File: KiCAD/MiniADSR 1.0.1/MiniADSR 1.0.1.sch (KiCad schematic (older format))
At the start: 35 parts, among them J1 INPUT, J2 OUTPUT, J4 ControlBoard_Pins, J6 MainBoard_Pins, Q1 BC547, Q2 BC547, Q3 BC547, U1 LM555xN, U2 TL072

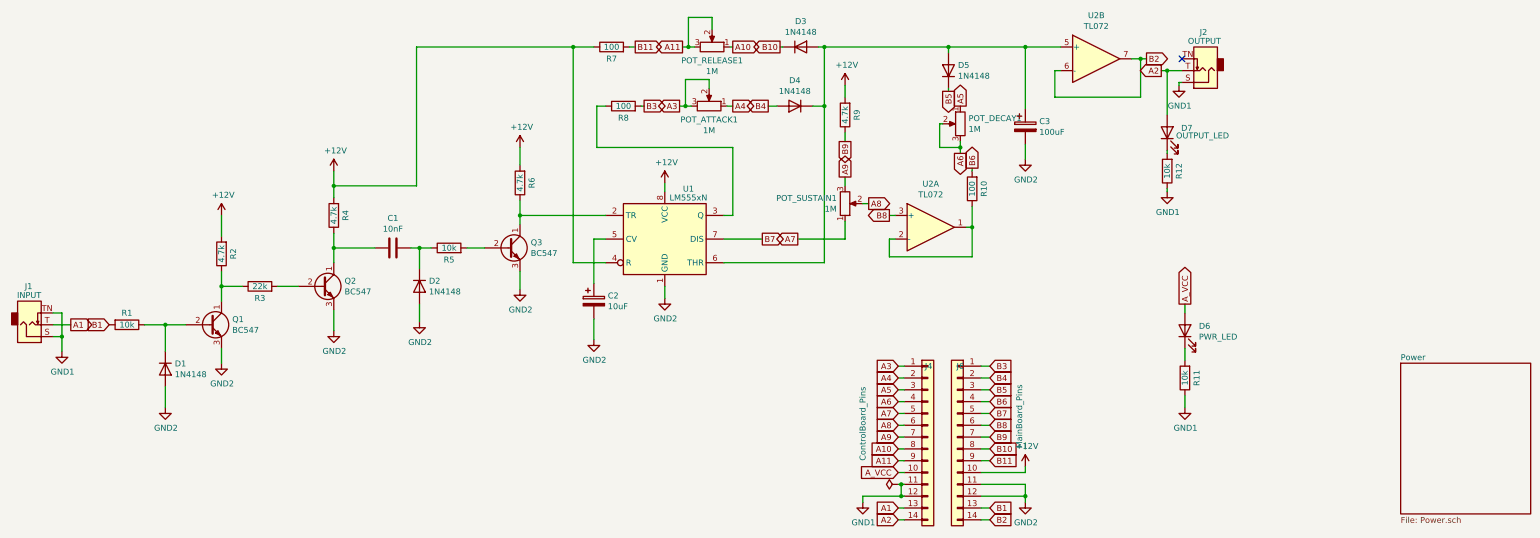
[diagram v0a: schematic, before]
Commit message: Added v1.0.1 for minor corrections on first version
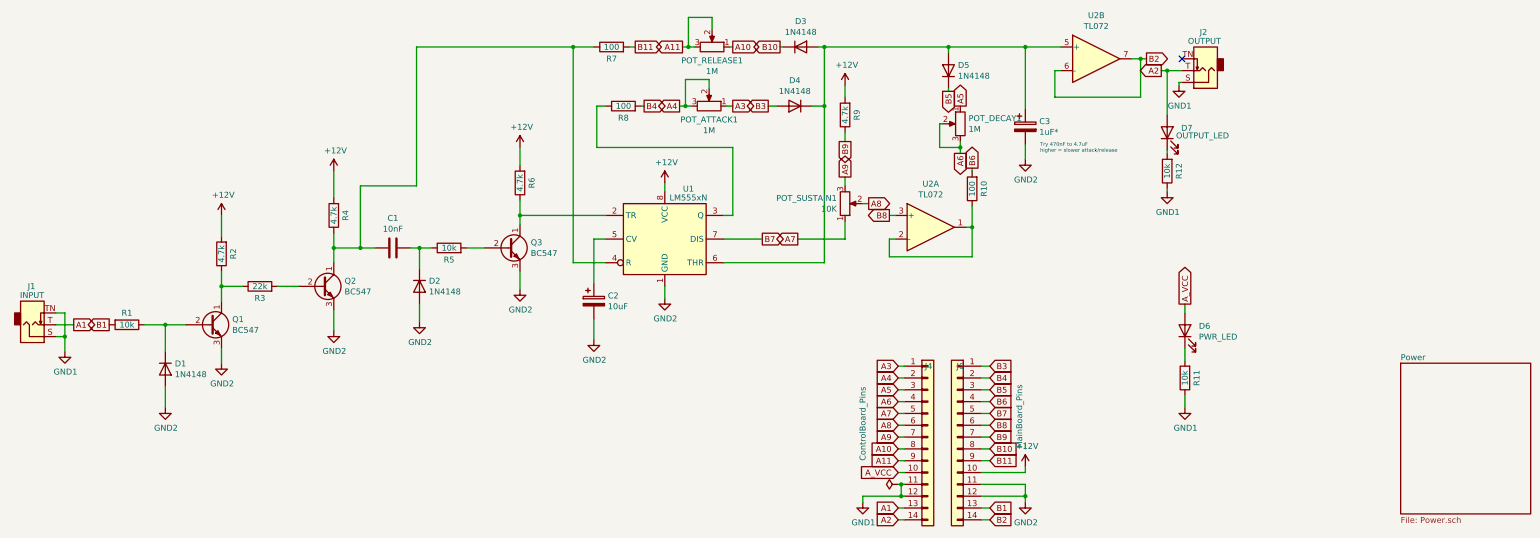
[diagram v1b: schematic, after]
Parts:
- C3: value 100uF -> 1uF*
- POT_SUSTAIN1: value 1M -> 10K
- Q1, Q2, Q3: footprint Package_TO_SOT_THT:TO-92_Inline -> Package_TO_SOT_THT:TO-92_Inline_Wide
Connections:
- net +12V: no longer R7.1, U1.4 (R)
- net A3: now also POT_ATTACK1.1; no longer POT_ATTACK1.2, POT_ATTACK1.3
- net A4: now also POT_ATTACK1.2, POT_ATTACK1.3; no longer POT_ATTACK1.1
- net B3: now also D4.2 (A); no longer R8.2
- net B4: now also R8.2; no longer D4.2 (A)
- net at C1.2, Q2.1 (C), R4.1: now also R7.1, U1.4 (R)
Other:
- note added: "Try 470nF to 4.7uF\nhigher = slower attack/release"
- moved on the sheet: J1
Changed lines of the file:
@@
 Title ""
 Date ""
-Rev ""
-Comp ""
+Rev "v1.0.1"
+Comp "benjiaomodular"
 Comment1 ""
 Comment2 ""
@@
 F 0 "Q1" H 2566 4421 50  0000 L CNN
 F 1 "BC547" H 2566 4330 50  0000 L CNN
-F 2 "Package_TO_SOT_THT:TO-92_Inline" H 2575 4300 50  0001 L CIN
+F 2 "Package_TO_SOT_THT:TO-92_Inline_Wide" H 2575 4300 50  0001 L CIN
 F 3 "https://www.onsemi.com/pub/Collateral/BC550-D.pdf" H 2375 4375 50  0001 L CNN
 	1    2375 4375
@@
 F 0 "Q2" H 3516 4096 50  0000 L CNN
 F 1 "BC547" H 3516 4005 50  0000 L CNN
-F 2 "Package_TO_SOT_THT:TO-92_Inline" H 3525 3975 50  0001 L CIN
+F 2 "Package_TO_SOT_THT:TO-92_Inline_Wide" H 3525 3975 50  0001 L CIN
 F 3 "https://www.onsemi.com/pub/Collateral/BC550-D.pdf" H 3325 4050 50  0001 L CNN
 	1    3325 4050
@@
 F 0 "Q3" H 5091 3771 50  0000 L CNN
 F 1 "BC547" H 5091 3680 50  0000 L CNN
-F 2 "Package_TO_SOT_THT:TO-92_Inline" H 5100 3650 50  0001 L CIN
+F 2 "Package_TO_SOT_THT:TO-92_Inline_Wide" H 5100 3650 50  0001 L CIN
 F 3 "https://www.onsemi.com/pub/Collateral/BC550-D.pdf" H 4900 3725 50  0001 L CNN
 	1    4900 3725
@@
 	2000 4375 2175 4375
 Wire Wire Line
-	1050 4375 1200 4375
+	1075 4375 1225 4375
 $Comp
 L power:GND2 #PWR06
@@
 	3425 3600 3425 3725
 Wire Wire Line
-	3775 3725 3425 3725
+	3775 3725 3650 3725
 Connection ~ 3425 3725
 Wire Wire Line
@@
 	1    0    0    -1
 $EndComp
-Wire Wire Line
-	3425 3075 3425 3200
 $Comp
 L power:+12V #PWR08
@@
 Wire Wire Line
 	4125 2025 4125 3200
-Wire Wire Line
-	4125 3200 3425 3200
 Connection ~ 5450 2025
-Connection ~ 3425 3200
-Wire Wire Line
-	3425 3200 3425 3300
 Wire Wire Line
 	5725 2525 5650 2525
@@
 P 7750 3350
 F 0 "POT_SUSTAIN1" H 7680 3304 50  0000 R CNN
-F 1 "1M" H 7680 3395 50  0000 R CNN
+F 1 "10K" H 7680 3395 50  0000 R CNN
 F 2 "benjiaomodular:Potentiometer_RV09" H 7750 3350 50  0001 C CNN
 F 3 "~" H 7750 3350 50  0001 C CNN
@@
 P 9275 2700
 F 0 "C3" H 9393 2746 50  0000 L CNN
-F 1 "100uF" H 9393 2655 50  0000 L CNN
+F 1 "1uF*" H 9393 2655 50  0000 L CNN
 F 2 "Capacitor_THT:CP_Radial_D5.0mm_P2.50mm" H 9313 2550 50  0001 C CNN
 F 3 "~" H 9275 2700 50  0001 C CNN
@@
 	9275 2025 9575 2025
 Wire Wire Line
-	1125 4475 1125 4600
+	1150 4475 1150 4600
 $Sheet
 S 12450 4700 1100 1275
@@
 	10625 4575 10625 4675
 Wire Wire Line
-	1125 4475 1050 4475
-Wire Wire Line
-	1050 4275 1125 4275
-Wire Wire Line
-	1125 4275 1125 4475
-Connection ~ 1125 4475
+	1150 4475 1075 4475
+Wire Wire Line
+	1075 4275 1150 4275
+Wire Wire Line
+	1150 4275 1150 4475
+Connection ~ 1150 4475
 $Comp
 L Connector:AudioJack2_SwitchT J1
 U 1 1 61DE2DCA
-P 850 4375
-F 0 "J1" H 875 4050 50  0000 R CNN
-F 1 "INPUT" H 950 4125 50  0000 R CNN
-F 2 "benjiaomodular:AudioJack_3.5mm" H 850 4375 50  0001 C CNN
-F 3 "~" H 850 4375 50  0001 C CNN
-	1    850  4375
+P 875 4375
+F 0 "J1" H 900 4050 50  0000 R CNN
+F 1 "INPUT" H 975 4125 50  0000 R CNN
+F 2 "benjiaomodular:AudioJack_3.5mm" H 875 4375 50  0001 C CNN
+F 3 "~" H 875 4375 50  0001 C CNN
+	1    875  4375
 	1    0    0    1
 $EndComp
-Text GLabel 1200 4375 2    50   Output ~ 0
+Text GLabel 1225 4375 2    50   Output ~ 0
 A1
-Text GLabel 1525 4375 0    50   Input ~ 0
+Text GLabel 1525 4375 0    50   Output ~ 0
 B1
 Text GLabel 10300 2125 2    50   Output ~ 0
@@
 L power:GND1 #PWR01
 U 1 1 61F0882F
-P 1125 4600
-F 0 "#PWR01" H 1125 4350 50  0001 C CNN
-F 1 "GND1" H 1130 4427 50  0000 C CNN
-F 2 "" H 1125 4600 50  0001 C CNN
-F 3 "" H 1125 4600 50  0001 C CNN
-	1    1125 4600
-	1    0    0    -1
-$EndComp
-Text GLabel 6350 2525 0    50   Output ~ 0
+P 1150 4600
+F 0 "#PWR01" H 1150 4350 50  0001 C CNN
+F 1 "GND1" H 1155 4427 50  0000 C CNN
+F 2 "" H 1150 4600 50  0001 C CNN
+F 3 "" H 1150 4600 50  0001 C CNN
+	1    1150 4600
+	1    0    0    -1
+$EndComp
+Text GLabel 6800 2525 2    50   Output ~ 0
 A3
 Wire Wire Line
 	6350 2525 6400 2525
 Connection ~ 6400 2525
-Text GLabel 6050 2525 2    50   Output ~ 0
+Text GLabel 7100 2525 0    50   Output ~ 0
 B3
 Wire Wire Line
 	6050 2525 6025 2525
-Text GLabel 6800 2525 2    50   Output ~ 0
+Text GLabel 6350 2525 0    50   Output ~ 0
 A4
 Wire Wire Line
@@
 	-1   0    0    1
 $EndComp
-Text GLabel 7100 2525 0    50   Output ~ 0
+Text GLabel 6050 2525 2    50   Output ~ 0
 B4
 Wire Wire Line
@@
 Wire Wire Line
 	7200 2025 7225 2025
+Wire Wire Line
+	3425 3075 3425 3300
+Wire Wire Line
+	4125 3200 3650 3200
+Wire Wire Line
+	3650 3200 3650 3725
+Connection ~ 3650 3725
+Wire Wire Line
+	3650 3725 3425 3725
+Text Notes 9400 2925 0    31   ~ 0
+Try 470nF to 4.7uF\nhigher = slower attack/release
 $EndSCHEMATC
